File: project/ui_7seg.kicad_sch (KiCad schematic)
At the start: 7 parts, among them U201 MAX7219, U202 3641AS, U203 3641AS

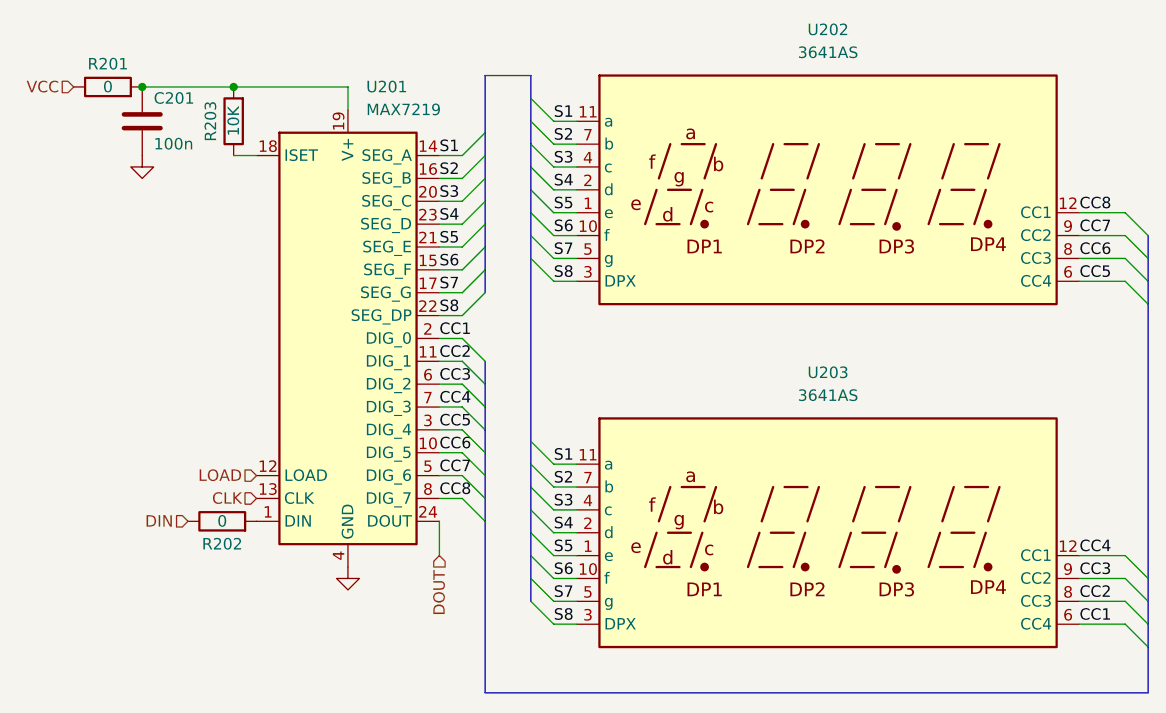
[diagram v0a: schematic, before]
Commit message: rs485 connector and minor silkscreen and led values fixes
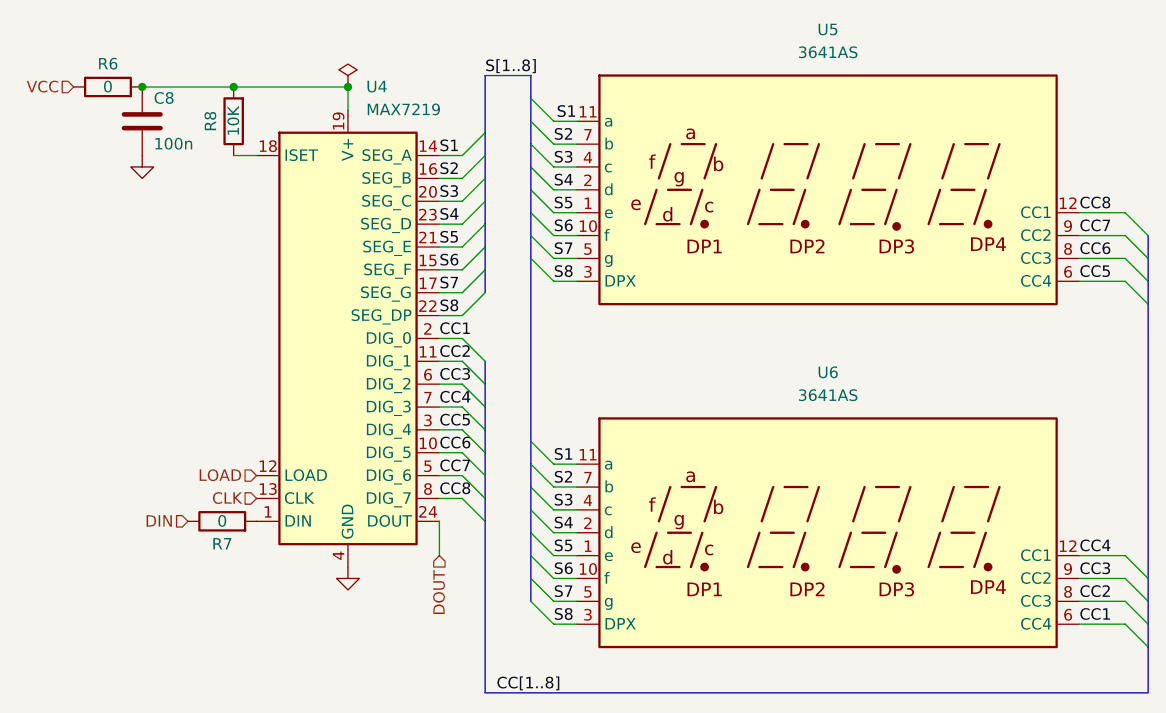
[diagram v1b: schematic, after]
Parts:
- renumbered C201 to C8, R201 to R6, R202 to R7, R203 to R8, U201 to U4, U202 to U5, U203 to U6
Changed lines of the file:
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@@
   (title_block
     (title "DZF-6020-UV-power-addon / UI board")
-    (date "2024-09-10")
-    (rev "1.0")
+    (date "2024-11-15")
+    (rev "1.1")
   )
   (junction (at 73.66 64.77) (diameter 0) (color 0 0 0 0)
@@
   (junction (at 63.5 64.77) (diameter 0) (color 0 0 0 0)
   )
+  (junction (at 86.36 64.77) (diameter 0) (color 0 0 0 0)
+  )
   (bus_entry (at 109.22 121.92) (size -2.54 -2.54)
     (stroke (width 0) (type default) (color 0 0 0 0))
@@
     (stroke (width 0) (type default) (color 0 0 0 0))
   )
+  (wire (pts (xy 109.22 68.58) (xy 111.76 68.58))
+    (stroke (width 0) (type default) (color 0 0 0 0))
+  )
   (wire (pts (xy 167.64 121.92) (xy 172.72 121.92))
     (stroke (width 0) (type default) (color 0 0 0 0))
@@
     (stroke (width 0) (type default) (color 0 0 0 0))
   )
-  (wire (pts (xy 109.22 68.58) (xy 111.76 68.58))
-    (stroke (width 0) (type default) (color 0 0 0 0))
-  )
   (bus (pts (xy 101.6 110.49) (xy 101.6 113.03))
     (stroke (width 0) (type default) (color 0 0 0 0))
@@
     (effects (font (size 1.27 1.27)) (justify left bottom))
   )
+  (label "S[1..8]" (at 101.6 63.5 0)
+    (effects (font (size 1.27 1.27)) (justify left bottom))
+  )
   (label "CC3" (at 167.64 119.38 0)
     (effects (font (size 1.27 1.27)) (justify left bottom))
@@
     (effects (font (size 1.27 1.27)) (justify left bottom))
   )
+  (label "CC[1..8]" (at 102.87 132.08 0)
+    (effects (font (size 1.27 1.27)) (justify left bottom))
+  )
   (label "S3" (at 96.52 77.47 0)
     (effects (font (size 1.27 1.27)) (justify left bottom))
@@
     (effects (font (size 1.27 1.27)) (justify left bottom))
   )
-  (label "S1" (at 109.22 68.58 0)
-    (effects (font (size 1.27 1.27)) (justify left bottom))
+  (label "S1" (at 111.76 68.58 180)
+    (effects (font (size 1.27 1.27)) (justify right bottom))
   )
   (label "S7" (at 96.52 87.63 0)
@@
   (symbol (lib_id "Display_Character:CC56-12EWA") (at 139.7 114.3 0) (unit 1)
     (in_bom yes) (on_board yes) (fields_autoplaced)
-    (property "Reference" "U203" (id 0) (at 139.7 96.52 0))
+    (property "Reference" "U6" (id 0) (at 139.7 96.52 0))
     (property "Value" "3641AS" (id 1) (at 139.7 99.06 0))
     (property "Footprint" "-local:3641AS" (id 2) (at 139.7 129.54 0)
@@
   (symbol (lib_id "Device:C") (at 63.5 68.58 0) (unit 1)
     (in_bom yes) (on_board yes)
-    (property "Reference" "C201" (id 0) (at 64.77 66.04 0)
+    (property "Reference" "C8" (id 0) (at 64.77 66.04 0)
       (effects (font (size 1.27 1.27)) (justify left))
     )
@@
   (symbol (lib_id "Device:R") (at 72.39 113.03 90) (unit 1)
     (in_bom yes) (on_board yes)
-    (property "Reference" "R202" (id 0) (at 72.39 115.57 90))
+    (property "Reference" "R7" (id 0) (at 72.39 115.57 90))
     (property "Value" "0" (id 1) (at 72.39 113.03 90))
     (property "Footprint" "Resistor_SMD:R_0805_2012Metric_Pad1.20x1.40mm_HandSolder" (id 2) (at 72.39 114.808 90)
@@
   (symbol (lib_id "power:GND") (at 86.36 118.11 0) (unit 1)
     (in_bom yes) (on_board yes) (fields_autoplaced)
-    (property "Reference" "#PWR0202" (id 0) (at 86.36 124.46 0)
+    (property "Reference" "#PWR013" (id 0) (at 86.36 124.46 0)
       (effects (font (size 1.27 1.27)) hide)
     )
@@
   (symbol (lib_id "power:GND") (at 63.5 72.39 0) (unit 1)
     (in_bom yes) (on_board yes) (fields_autoplaced)
-    (property "Reference" "#PWR0201" (id 0) (at 63.5 78.74 0)
+    (property "Reference" "#PWR012" (id 0) (at 63.5 78.74 0)
       (effects (font (size 1.27 1.27)) hide)
     )
@@
   (symbol (lib_id "Driver_LED:MAX7219") (at 86.36 92.71 0) (unit 1)
     (in_bom yes) (on_board yes) (fields_autoplaced)
-    (property "Reference" "U201" (id 0) (at 88.3794 64.77 0)
+    (property "Reference" "U4" (id 0) (at 88.3794 64.77 0)
       (effects (font (size 1.27 1.27)) (justify left))
     )
@@
   (symbol (lib_id "Display_Character:CC56-12EWA") (at 139.7 76.2 0) (unit 1)
     (in_bom yes) (on_board yes) (fields_autoplaced)
-    (property "Reference" "U202" (id 0) (at 139.7 58.42 0))
+    (property "Reference" "U5" (id 0) (at 139.7 58.42 0))
     (property "Value" "3641AS" (id 1) (at 139.7 60.96 0))
     (property "Footprint" "-local:3641AS" (id 2) (at 139.7 91.44 0)
@@
   (symbol (lib_id "Device:R") (at 73.66 68.58 180) (unit 1)
     (in_bom yes) (on_board yes)
-    (property "Reference" "R203" (id 0) (at 71.12 68.58 90))
+    (property "Reference" "R8" (id 0) (at 71.12 68.58 90))
     (property "Value" "10K" (id 1) (at 73.66 68.58 90))
     (property "Footprint" "Resistor_SMD:R_0805_2012Metric_Pad1.20x1.40mm_HandSolder" (id 2) (at 75.438 68.58 90)
@@
     (pin "2")
   )
+  (symbol (lib_id "power:PWR_FLAG") (at 86.36 64.77 0) (unit 1)
+    (in_bom yes) (on_board yes) (fields_autoplaced)
+    (property "Reference" "#FLG04" (id 0) (at 86.36 62.865 0)
+      (effects (font (size 1.27 1.27)) hide)
+    )
+    (property "Value" "PWR_FLAG" (id 1) (at 86.36 59.69 0)
+      (effects (font (size 1.27 1.27)) hide)
+    )
+    (property "Footprint" "" (id 2) (at 86.36 64.77 0)
+      (effects (font (size 1.27 1.27)) hide)
+    )
+    (property "Datasheet" "~" (id 3) (at 86.36 64.77 0)
+      (effects (font (size 1.27 1.27)) hide)
+    )
+    (pin "1")
+  )
   (symbol (lib_id "Device:R") (at 59.69 64.77 90) (unit 1)
     (in_bom yes) (on_board yes)
-    (property "Reference" "R201" (id 0) (at 59.69 62.23 90))
+    (property "Reference" "R6" (id 0) (at 59.69 62.23 90))
     (property "Value" "0" (id 1) (at 59.69 64.77 90))
     (property "Footprint" "Resistor_SMD:R_0805_2012Metric_Pad1.20x1.40mm_HandSolder" (id 2) (at 59.69 66.548 90)
